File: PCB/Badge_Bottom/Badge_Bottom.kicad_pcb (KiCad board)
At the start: 2 copper layers, 65 x 75 mm, 23 parts, among them CN1 PJ-320, CN2 PJ-320, J1 Conn_01x01, J1 USB_C_Receptacle_USB2.0, J2 Conn_01x01, J3 Conn_01x01, J3 Conn_01x01_Pin, J4 Conn_01x01, J5 Conn_01x01, J6 Conn_01x01, J7 Conn_01x01, J8 Conn_01x01, J9 Conn_01x01, Q1 AO3400A, SW1 TM-2024A, SW2 TM-2024A, SW3 MSK12C02-HB, U1 TP4054, U2 CH32V305RBT6, U3 AMS1117-3.3

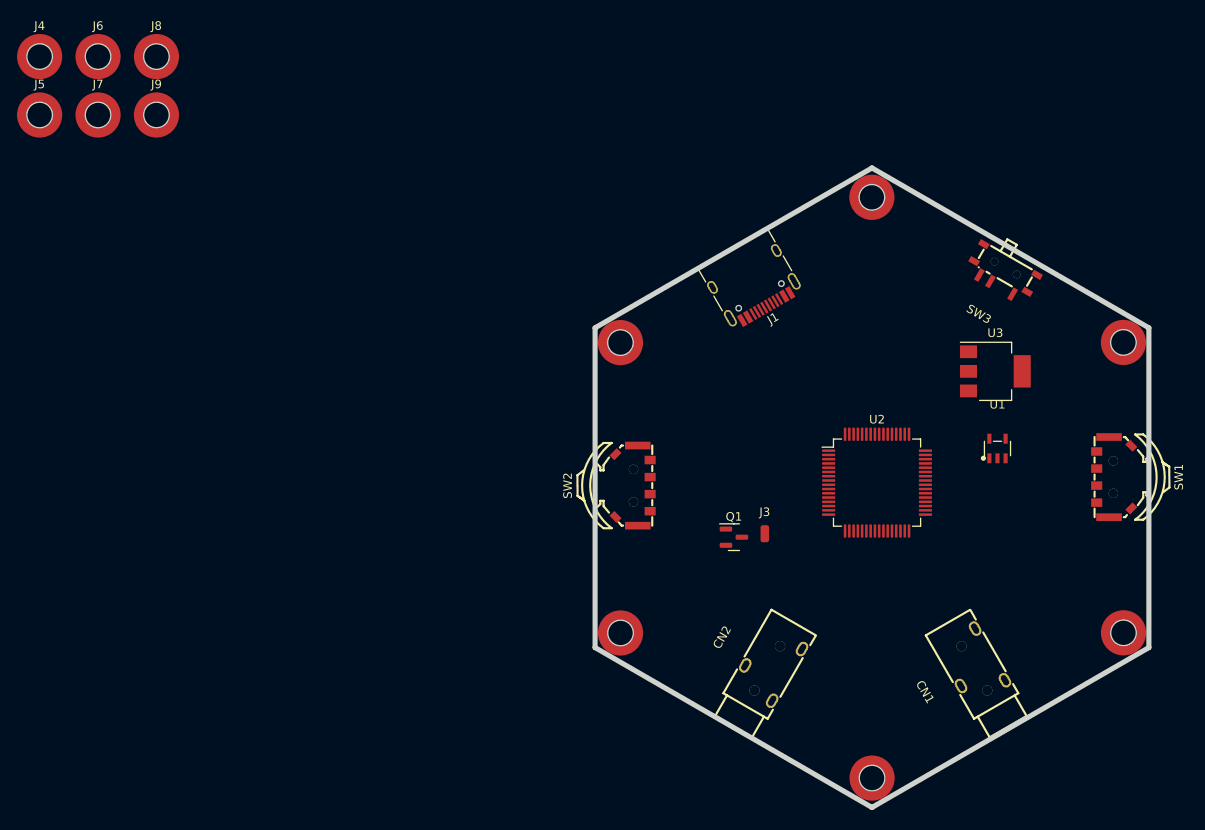
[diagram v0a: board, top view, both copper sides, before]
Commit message: Added new page for IO, added new components, added JLC parts, fixed PCB standoffs to be pads and modified concept of PCB (dual usbc)
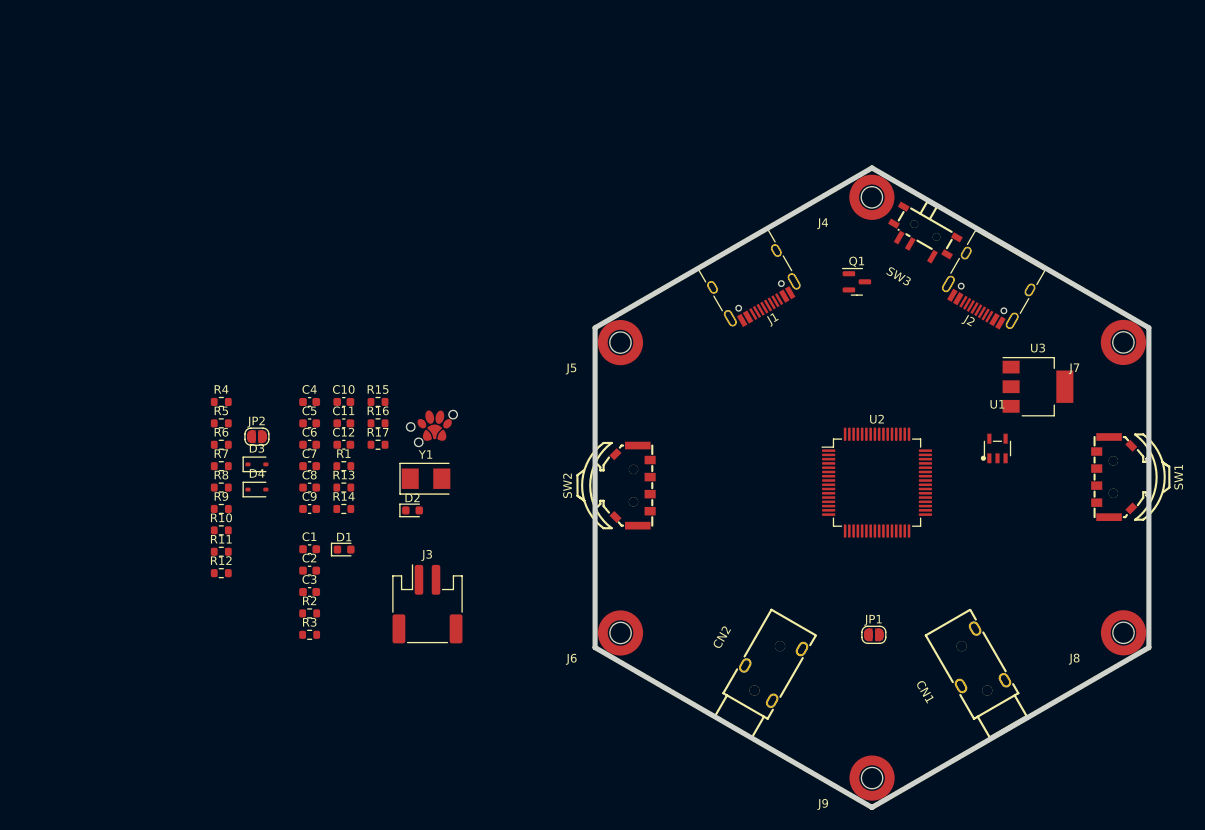
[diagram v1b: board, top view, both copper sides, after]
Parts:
- removed the J1 at (142.9, 64.3)
- removed the J3 at (172.4, 115.4)
- removed the J4 at (142.9, 132.4)
- removed the J5 at (113.4, 115.4)
- removed the J6 at (113.4, 81.3)
- added C1: 1u, Capacitor_SMD:C_0603_1608Metric, F.Cu at (77.0, 105.6)
- added C10: 0.1u, Capacitor_SMD:C_0603_1608Metric, F.Cu at (81.0, 88.3)
- added C11: 20p, Capacitor_SMD:C_0603_1608Metric, F.Cu at (81.0, 90.8)
- added C12: 20p, Capacitor_SMD:C_0603_1608Metric, F.Cu at (81.0, 93.3)
- added C2: 22u, Capacitor_SMD:C_0603_1608Metric, F.Cu at (77.0, 108.1)
- added C3: 1u, Capacitor_SMD:C_0603_1608Metric, F.Cu at (77.0, 110.6)
- added C4: 0.1u, Capacitor_SMD:C_0603_1608Metric, F.Cu at (77.0, 88.3)
- added C5: 0.1u, Capacitor_SMD:C_0603_1608Metric, F.Cu at (77.0, 90.8)
- added C6: 0.1u, Capacitor_SMD:C_0603_1608Metric, F.Cu at (77.0, 93.3)
- added C7: 0.1u, Capacitor_SMD:C_0603_1608Metric, F.Cu at (77.0, 95.8)
- added C8: 0.1u, Capacitor_SMD:C_0603_1608Metric, F.Cu at (77.0, 98.3)
- added C9: 0.1u, Capacitor_SMD:C_0603_1608Metric, F.Cu at (77.0, 100.8)
- added D1: CHG, LED_SMD:LED_0603_1608Metric, F.Cu at (81.0, 105.6)
- added D2: USER, LED_SMD:LED_0603_1608Metric, F.Cu at (89.0, 101.0)
- added D3: 1N5819, Diode_SMD:D_SOD-323, F.Cu at (70.8, 95.6)
- added D4: 1N5819, Diode_SMD:D_SOD-323, F.Cu at (70.8, 98.6)
- added J10: Debug, Paw-Connect_RevB_TC2030-IDC-NL_2x03_P1.27mm_Vertical:Paw-Connect_RevB_TC2030-IDC-NL_2x03_P1.27mm_Vertical, F.Cu at (91.3, 91.4)
- added JP1: SolderJumper_2_Open, Jumper:SolderJumper-2_P1.3mm_Open_RoundedPad1.0x1.5mm, F.Cu at (143.2, 115.6)
- added JP2: SolderJumper_2_Open, Jumper:SolderJumper-2_P1.3mm_Open_RoundedPad1.0x1.5mm, F.Cu at (70.8, 92.4)
- added R1: 10k, Resistor_SMD:R_0603_1608Metric, F.Cu at (81.0, 95.8)
- added R10: 5k1, Resistor_SMD:R_0603_1608Metric, F.Cu at (66.6, 103.3)
- added R11: 5k1, Resistor_SMD:R_0603_1608Metric, F.Cu at (66.6, 105.9)
- added R12: 10k, Resistor_SMD:R_0603_1608Metric, F.Cu at (66.6, 108.4)
- added R13: 1M, Resistor_SMD:R_0603_1608Metric, F.Cu at (81.0, 98.3)
- added R14: 1M, Resistor_SMD:R_0603_1608Metric, F.Cu at (81.0, 100.8)
- added R15: 10k, Resistor_SMD:R_0603_1608Metric, F.Cu at (85.0, 88.3)
- added R16: 10k, Resistor_SMD:R_0603_1608Metric, F.Cu at (85.0, 90.8)
- added R17: 1k, Resistor_SMD:R_0603_1608Metric, F.Cu at (85.0, 93.3)
- added R2: 1.65k, Resistor_SMD:R_0603_1608Metric, F.Cu at (77.0, 113.1)
- added R3: 330, Resistor_SMD:R_0603_1608Metric, F.Cu at (77.0, 115.6)
- added R4: 100, Resistor_SMD:R_0603_1608Metric, F.Cu at (66.6, 88.3)
- added R5: 100, Resistor_SMD:R_0603_1608Metric, F.Cu at (66.6, 90.8)
- added R6: 100, Resistor_SMD:R_0603_1608Metric, F.Cu at (66.6, 93.3)
- added R7: 100, Resistor_SMD:R_0603_1608Metric, F.Cu at (66.6, 95.8)
- added R8: 5k1, Resistor_SMD:R_0603_1608Metric, F.Cu at (66.6, 98.3)
- added R9: 5k1, Resistor_SMD:R_0603_1608Metric, F.Cu at (66.6, 100.8)
- added Y1: 8M, Crystal:Crystal_SMD_5032-2Pin_5.0x3.2mm, F.Cu at (90.6, 97.3)
- CN1: value PJ-320 -> JACK_IN
- CN2: value PJ-320 -> JACK_OUT
- J1: value USB_C_Receptacle_USB2.0 -> USB_FS
- J2: value Conn_01x01 -> USB_HS; footprint Mounting_Wuerth:Mounting_Wuerth_WA-SMSI-M2_H7mm_9774070243 -> Connector_USB:USB_C_Receptacle_HRO_TYPE-C-31-M-12
- J3: value Conn_01x01_Pin -> BAT; footprint Connector_Wire:SolderWirePad_1x01_SMD_1x2mm -> Connector_JST:JST_PH_S2B-PH-SM4-TB_1x02-1MP_P2.00mm_Horizontal
- J4, J6, J8: value Conn_01x01 -> Nylon Screw; footprint Mounting_Wuerth:Mounting_Wuerth_WA-SMSI-M2_H7mm_9774070243 -> standoff_pad_m2:Standoff_Pad_M2
- J5, J7, J9: value Conn_01x01 -> Metal Screw; footprint Mounting_Wuerth:Mounting_Wuerth_WA-SMSI-M2_H7mm_9774070243 -> standoff_pad_m2:Standoff_Pad_M2
- moved J8 132.0 mm to (172.4, 115.4)
- moved J7 123.2 mm to (172.4, 81.3)
- moved J9 114.4 mm to (142.9, 132.4)
- moved J4 99.0 mm to (142.9, 64.3)
- moved J6 91.2 mm to (113.4, 115.4)
- moved J5 73.2 mm to (113.4, 81.3)
- moved J3 40.4 mm to (90.8, 112.0)
- moved Q1 33.2 mm to (141.2, 74.2)
- moved J2 16.9 mm to (157.2, 73.9), turned to 150 degrees
- moved SW3 10.4 mm to (148.9, 68.7)
- moved U3 5.31 mm to (162.4, 86.5)
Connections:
- CN1 pad 2: unconnected-(CN1-Pad2) -> Net-(CN1-Pad2)
- CN1 pad 3: unconnected-(CN1-Pad3) -> GND
- CN1 pad 4: unconnected-(CN1-Pad4) -> Net-(CN1-Pad4)
- CN2 pad 2: unconnected-(CN2-Pad2) -> Net-(CN2-Pad2)
- CN2 pad 3: unconnected-(CN2-Pad3) -> GND
- CN2 pad 4: unconnected-(CN2-Pad4) -> Net-(CN2-Pad4)
- J1 pad A4: VBUS -> Net-(D3-A)
- J1 pad A5: unconnected-(J1-CC1-PadA5) -> Net-(J1-CC1)
- J1 pad A6: unconnected-(J1-D+-PadA6) -> PA12-USBFS_DP
- J1 pad A7: unconnected-(J1-D--PadA7) -> PA11-USBFS_DM
- J1 pad A9: VBUS -> Net-(D3-A)
- J1 pad B4: VBUS -> Net-(D3-A)
- J1 pad B5: unconnected-(J1-CC2-PadB5) -> Net-(J1-CC2)
- J1 pad B6: unconnected-(J1-D+-PadB6) -> PA12-USBFS_DP
- J1 pad B7: unconnected-(J1-D--PadB7) -> PA11-USBFS_DM
- J1 pad B9: VBUS -> Net-(D3-A)
- J3 pad 1: unconnected-(J3-Pin_1-Pad1) -> +BATT
- J4 pad 1: GND -> Net-(J4-Pin_1)
- J5 pad 1: DOUT -> unconnected-(J5-Pin_1-Pad1)
- J6 pad 1: DIN -> PA8-TIM1
- Q1 pad 1: unconnected-(Q1-G-Pad1) -> PA6-LEDFET
- Q1 pad 2: unconnected-(Q1-S-Pad2) -> GND
- Q1 pad 3: unconnected-(Q1-D-Pad3) -> Net-(J4-Pin_1)
- SW1 pad 3: unconnected-(SW1-Pad3) -> BOOT0
- SW1 pad 4: unconnected-(SW1-Pad4) -> +3V3
- SW3 pad 2: VCC -> VDD
- U2 pad 10: unconnected-(U2-PC2-Pad10) -> PC2-GPIO
- U2 pad 11: unconnected-(U2-PC3-Pad11) -> PC3-GPIO
- U2 pad 12: unconnected-(U2-VSSA-Pad12) -> GND
- U2 pad 13: unconnected-(U2-VDDA-Pad13) -> +3V3
- U2 pad 14: unconnected-(U2-PA0/WAKEUP-Pad14) -> PA0-GPIO
- U2 pad 15: unconnected-(U2-PA1-Pad15) -> PA1-ADC_IN1
- U2 pad 16: unconnected-(U2-PA2-Pad16) -> PA2-ADC_IN2/USART2_TX
- U2 pad 17: unconnected-(U2-PA3-Pad17) -> PA3-ADC_IN_3/USART2_RX
- U2 pad 18: unconnected-(U2-VSS-Pad18) -> GND
- U2 pad 19: unconnected-(U2-VDD-Pad19) -> +3V3
- U2 pad 2: unconnected-(U2-PC13/TAMPER-RTC-Pad2) -> PC13-GPIO
- U2 pad 20: unconnected-(U2-PA4-Pad20) -> PA4-DAC1
- U2 pad 21: unconnected-(U2-PA5-Pad21) -> PA10-USART1_RX
- U2 pad 22: unconnected-(U2-PA6-Pad22) -> PA6-LEDFET
- U2 pad 23: unconnected-(U2-PA7-Pad23) -> Net-(D2-A)
- U2 pad 24: unconnected-(U2-PC4-Pad24) -> PC4-GPIO
- U2 pad 25: unconnected-(U2-PC5-Pad25) -> PC5-GPIO
- U2 pad 26: unconnected-(U2-PB0-Pad26) -> PB0-UART4_TX
- U2 pad 27: unconnected-(U2-PB1-Pad27) -> PB1-UART4_RX
- U2 pad 28: unconnected-(U2-PB2-Pad28) -> Net-(U2-BOOT1/PB2)
- U2 pad 29: unconnected-(U2-PB10-Pad29) -> PB10-BTNR_BTN
- U2 pad 3: unconnected-(U2-PC14/OSC32_IN-Pad3) -> PC14-GPIO
- U2 pad 30: unconnected-(U2-PB11-Pad30) -> PB11-BTNR_UP
- U2 pad 31: unconnected-(U2-VSS-Pad31) -> GND
- U2 pad 32: unconnected-(U2-VIO-Pad32) -> +3V3
- U2 pad 33: unconnected-(U2-PB12-Pad33) -> PB12-BNTR_DOWN
- U2 pad 34: unconnected-(U2-PB13-Pad34) -> PB13-BTNL-BTN
- U2 pad 35: unconnected-(U2-PB14-Pad35) -> PB14-BTNL_UP
- U2 pad 36: unconnected-(U2-PB15-Pad36) -> PB15-BTNL_DOWN
- U2 pad 37: unconnected-(U2-PC6-Pad37) -> PC6-GPIO
- U2 pad 38: unconnected-(U2-PC7-Pad38) -> PC7-GPIO
- U2 pad 39: unconnected-(U2-PC8-Pad39) -> PC8-SDIO_D0
- U2 pad 4: unconnected-(U2-PC15/OSC32_OUT-Pad4) -> PC15-GPIO
- U2 pad 40: unconnected-(U2-PC9-Pad40) -> PC9-SDIO_D1
- U2 pad 41: unconnected-(U2-PA8-Pad41) -> PA8-TIM1
- U2 pad 42: unconnected-(U2-PA9-Pad42) -> PA4-DAC1
- U2 pad 43: unconnected-(U2-PA10-Pad43) -> PA10-USART1_RX
- U2 pad 44: unconnected-(U2-PA11-Pad44) -> PA11-USBFS_DM
- U2 pad 45: unconnected-(U2-PA12-Pad45) -> PA12-USBFS_DP
- U2 pad 46: unconnected-(U2-PA13-Pad46) -> PA13-SWD
- U2 pad 47: unconnected-(U2-VSS-Pad47) -> GND
- U2 pad 48: unconnected-(U2-VDD-Pad48) -> +3V3
- U2 pad 49: unconnected-(U2-PA14-Pad49) -> PA14-SWCLK
- U2 pad 5: unconnected-(U2-OSC_IN-Pad5) -> Net-(U2-OSC_IN)
- U2 pad 50: unconnected-(U2-PA15-Pad50) -> PA15-SPI1_NSS
- U2 pad 51: unconnected-(U2-PC10-Pad51) -> PC10-SDIO_D2
- U2 pad 52: unconnected-(U2-PC11-Pad52) -> PC11-SDIO_D3
- U2 pad 53: unconnected-(U2-PC12-Pad53) -> PC12-SDIO_CLK
- U2 pad 54: unconnected-(U2-PD2-Pad54) -> PD2-SDIO_CMD
- U2 pad 55: unconnected-(U2-PB3-Pad55) -> PB3-SPI1_SCK
- U2 pad 56: unconnected-(U2-PB4-Pad56) -> PB4-SPI1_MISO
- U2 pad 57: unconnected-(U2-PB5-Pad57) -> PB5-SPI1_MOSI
- U2 pad 58: unconnected-(U2-PB6-Pad58) -> PB6-USBHS_DM
- U2 pad 59: unconnected-(U2-PB7-Pad59) -> PB7-USBHS_DP
- U2 pad 6: unconnected-(U2-OSC_OUT-Pad6) -> Net-(U2-OSC_OUT)
- U2 pad 60: unconnected-(U2-BOOT-Pad60) -> BOOT0
- U2 pad 61: unconnected-(U2-PB8-Pad61) -> PB8-I2C_SCL
- U2 pad 62: unconnected-(U2-PB9-Pad62) -> PB8-I2C_SDA
- U2 pad 63: unconnected-(U2-VSS-Pad63) -> GND
- U2 pad 64: unconnected-(U2-VIO-Pad64) -> +3V3
- U2 pad 7: unconnected-(U2-NRST-Pad7) -> NRST
- U2 pad 8: unconnected-(U2-PC0-Pad8) -> PC0-GPIO
- U2 pad 9: unconnected-(U2-PC1-Pad9) -> PC1-GPIO
- U3 pad 3: VCC -> VDD
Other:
- board text added: "TODO: - route gpios out to 2x2 pinheaders, some with vcc and gnd (sao) - check with flower badge team for pinout of headphone jack - routing - bom and hope - don't forget external stuff, like battery and few replacement parts like buttons and switches - review schematic and pcb before buy!"
- board text removed: "TODO: - replace standoffs with holes and a copper pad for electrical contact - two usb-c, hide switch - route gpios out to 2x2 pinheaders, some with vcc and gnd (sao) - check with flower badge team for pinout of headphone jack"
